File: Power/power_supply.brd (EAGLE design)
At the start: 100 x 80 mm, 10 parts

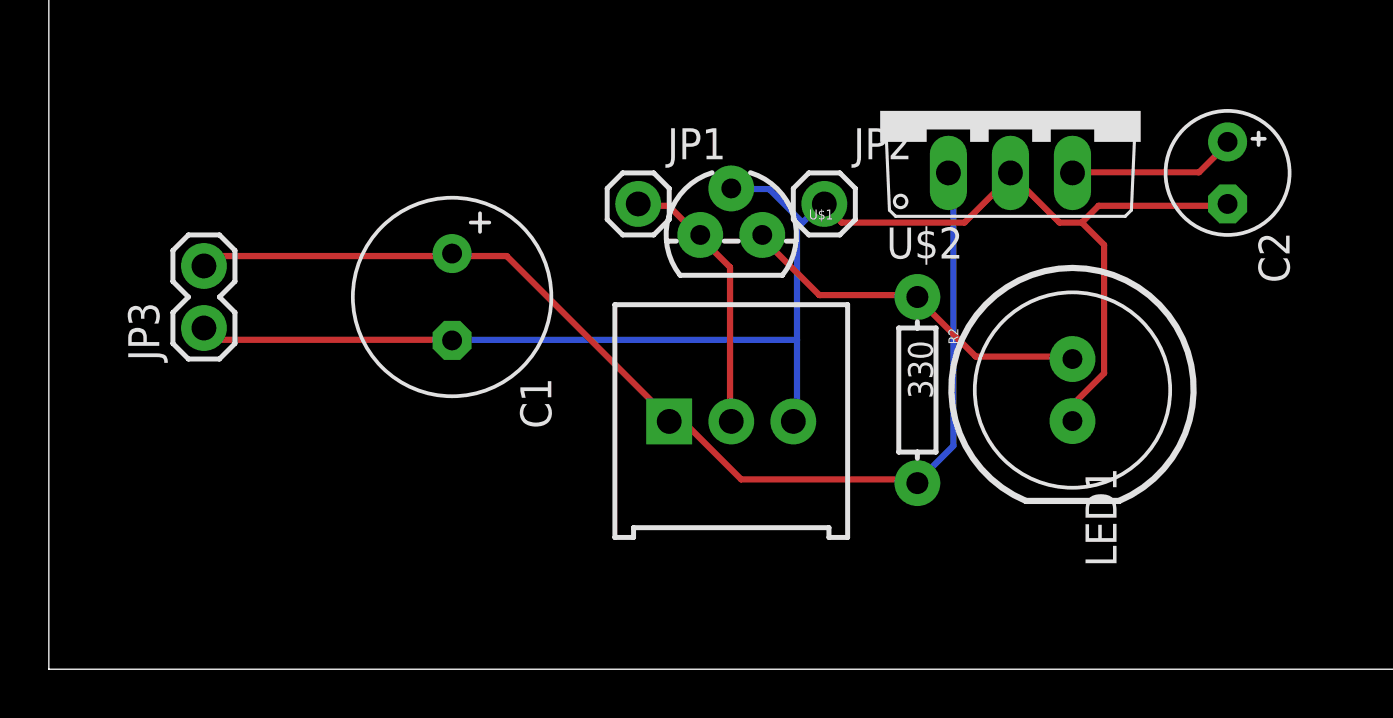
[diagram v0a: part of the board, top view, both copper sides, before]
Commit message: Changes to the Power Supply
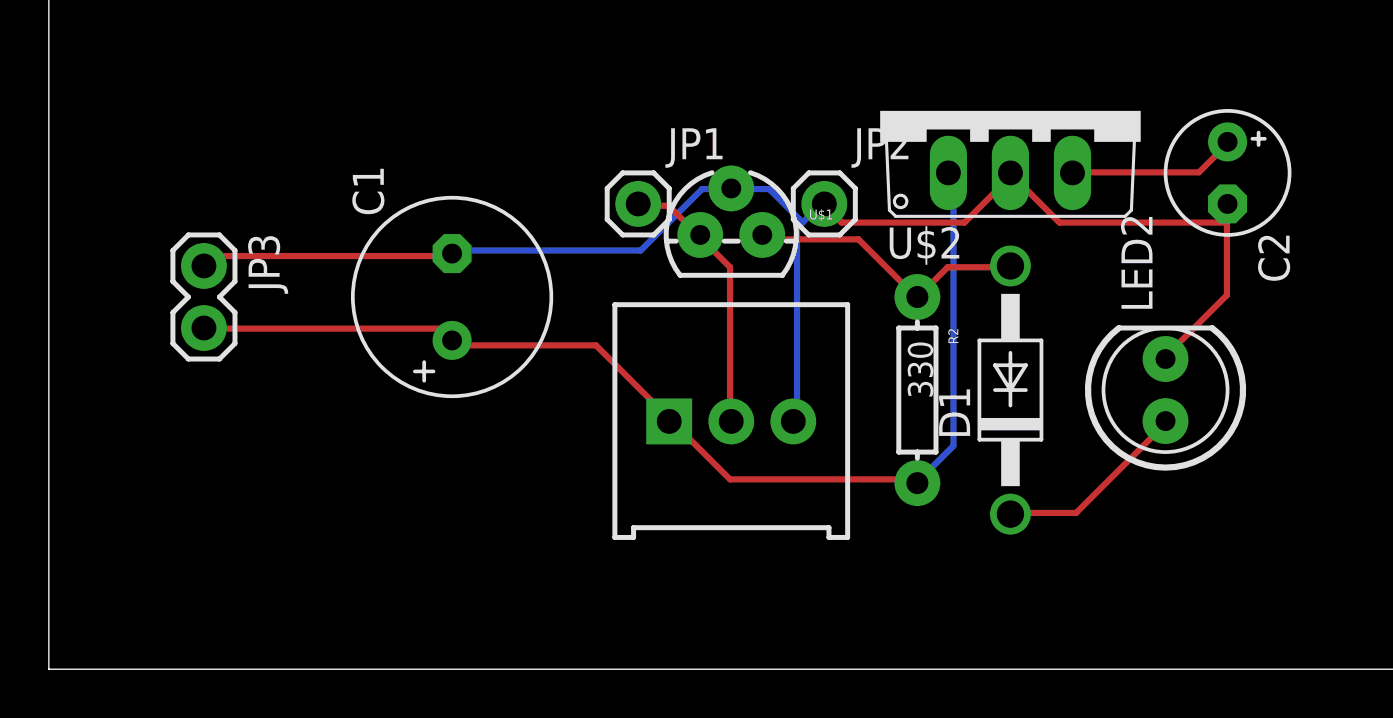
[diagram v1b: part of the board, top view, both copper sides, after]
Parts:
- removed LED1: Green/Yellow, SparkFun:LED10MM-2
- added D1: 1N4001, diode:DO41-10
- added LED2: Yellow/Multi, SparkFun:LED5MM
- moved JP3 2.54 mm to (6.35, 16.5), turned to 270 degrees
- turned C1 to 90 degrees
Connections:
- new net N$1: D1.C, LED2.A
- net GND: now also LED2.K; no longer LED1.K
- net N$2: now also D1.A; no longer LED1.A
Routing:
- net N$1: track 0.00 -> 7.97 mm
- net N$2: track 14.9 -> 11.8 mm
- net GND: track 65.5 -> 62.7 mm
- net VCC: track 46.8 -> 45.3 mm

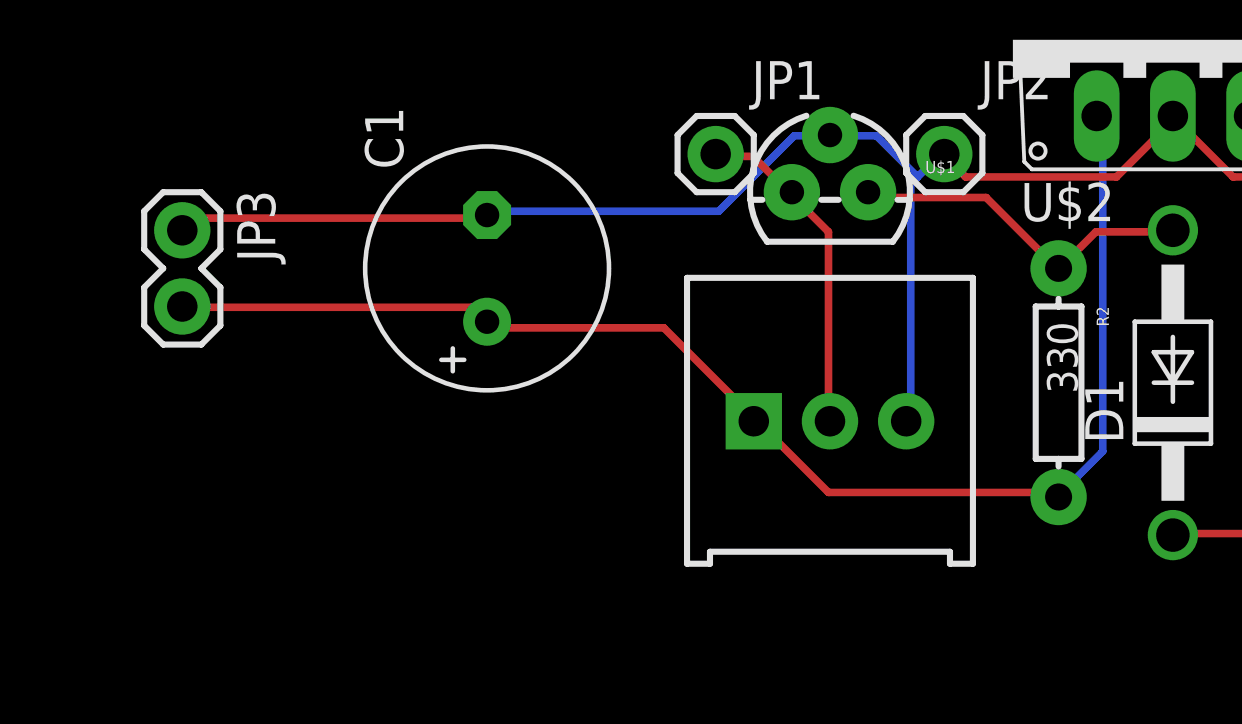
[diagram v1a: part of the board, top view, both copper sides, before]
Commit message: Updated the POT package
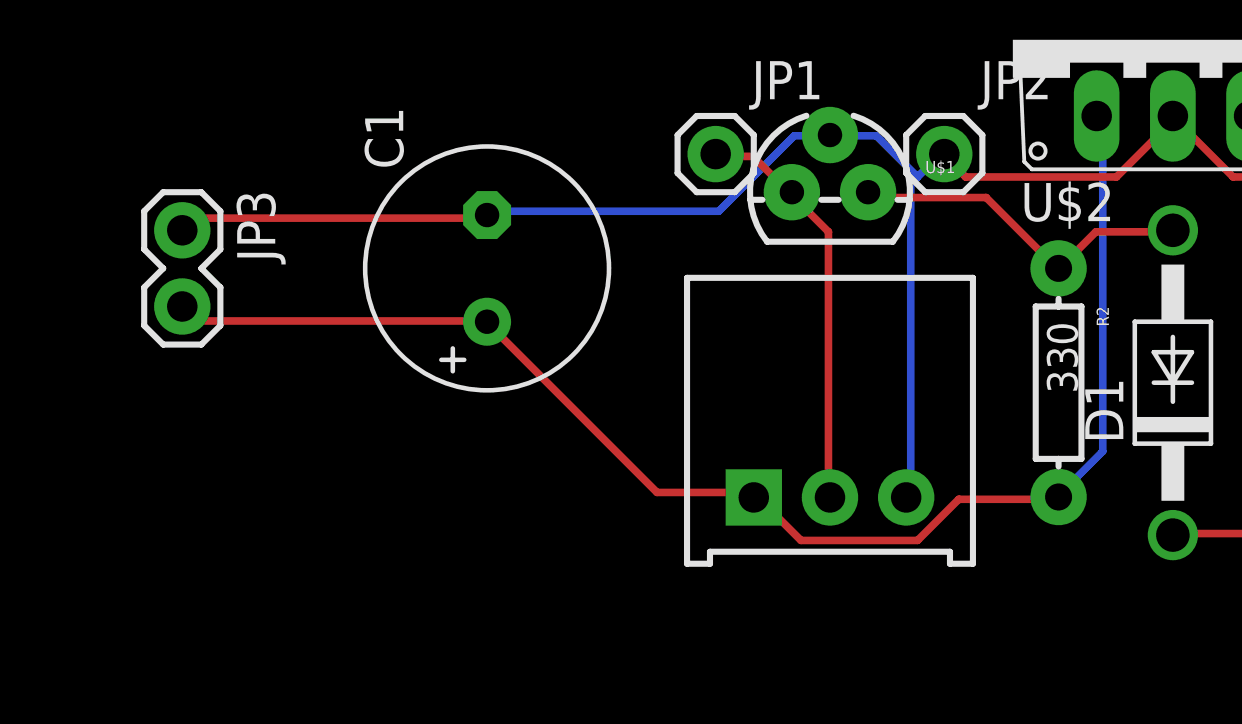
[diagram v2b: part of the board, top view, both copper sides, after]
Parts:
- R1: device SparkFun:3386U -> Power:3386U
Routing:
- net VCUTOFF: track 11.2 -> 13.7 mm
- net GND: track 62.7 -> 65.2 mm
- net VCC: track 45.3 -> 46.5 mm
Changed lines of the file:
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@@
 <element name="JP2" library="SparkFun" package="1X01" value="M01PTH" x="31.75" y="19.05"/>
 <element name="JP3" library="SparkFun" package="1X02" value="Battery" x="6.35" y="16.51" rot="R270"/>
-<element name="R1" library="SparkFun" package="3386U" value="10K" x="27.94" y="10.16"/>
 <element name="R2" library="SparkFun" package="AXIAL-0.3" value="330" x="35.56" y="11.43" rot="R270"/>
 <element name="U$1" library="SparkFun" package="TO-92" value="TL431PTH" x="27.94" y="17.78"/>
@@
 <element name="D1" library="diode" package="DO41-10" value="1N4001" x="39.37" y="11.43" rot="R90"/>
 <element name="LED2" library="SparkFun" package="LED5MM" value="Yellow/Multi" x="45.72" y="11.43" rot="R90"/>
+<element name="R1" library="Power" package="3386U" value="10K" x="27.94" y="10.16">
+<attribute name="CREATOR" value="Brandon" x="27.94" y="10.16" size="1.778" layer="27" display="off"/>
+<attribute name="REVIEWER1" value="Chris" x="27.94" y="10.16" size="1.778" layer="27" display="off"/>
+</element>
 </elements>
 <signals>
@@
 <contactref element="JP2" pad="1"/>
 <contactref element="U$1" pad="2"/>
-<contactref element="R1" pad="3"/>
 <contactref element="JP3" pad="1"/>
 <contactref element="U$2" pad="2"/>
@@
 <contactref element="C2" pad="-"/>
 <contactref element="LED2" pad="K"/>
+<contactref element="R1" pad="3"/>
 <wire x1="6.6294" y1="16.9164" x2="16.4592" y2="16.9164" width="0.254" layer="1"/>
 <wire x1="6.4008" y1="16.6878" x2="6.6294" y2="16.9164" width="0.254" layer="1"/>
@@
 <wire x1="39.3192" y1="20.1168" x2="39.37" y2="20.32" width="0.254" layer="1"/>
 <wire x1="31.7754" y1="18.9738" x2="31.75" y2="19.05" width="0.254" layer="1"/>
-<wire x1="30.6324" y1="18.0594" x2="30.6324" y2="10.287" width="0.254" layer="16"/>
+<wire x1="30.6324" y1="18.0594" x2="30.6324" y2="7.7724" width="0.254" layer="16"/>
 <wire x1="31.5468" y1="18.9738" x2="30.861" y2="18.288" width="0.254" layer="16"/>
 <wire x1="30.861" y1="18.288" x2="30.6324" y2="18.0594" width="0.254" layer="16"/>
-<wire x1="30.6324" y1="10.287" x2="30.48" y2="10.145" width="0.254" layer="16"/>
+<wire x1="30.6324" y1="7.7724" x2="30.48" y2="7.605" width="0.254" layer="16"/>
 <wire x1="31.5468" y1="18.9738" x2="31.75" y2="19.05" width="0.254" layer="16"/>
 <wire x1="29.4894" y1="19.6596" x2="28.1178" y2="19.6596" width="0.254" layer="16"/>
@@
 </signal>
 <signal name="VCUTOFF">
-<contactref element="R1" pad="2"/>
 <contactref element="U$1" pad="1"/>
 <contactref element="JP1" pad="1"/>
+<contactref element="R1" pad="2"/>
 <wire x1="25.3746" y1="18.9738" x2="24.2316" y2="18.9738" width="0.254" layer="1"/>
 <wire x1="26.5176" y1="17.8308" x2="25.3746" y2="18.9738" width="0.254" layer="1"/>
 <wire x1="24.2316" y1="18.9738" x2="24.13" y2="19.05" width="0.254" layer="1"/>
 <wire x1="26.5176" y1="17.8308" x2="26.67" y2="17.78" width="0.254" layer="1"/>
-<wire x1="27.8892" y1="16.4592" x2="27.8892" y2="10.287" width="0.254" layer="1"/>
+<wire x1="27.8892" y1="16.4592" x2="27.8892" y2="7.7724" width="0.254" layer="1"/>
 <wire x1="26.7462" y1="17.6022" x2="27.8892" y2="16.4592" width="0.254" layer="1"/>
-<wire x1="27.8892" y1="10.287" x2="27.94" y2="10.145" width="0.254" layer="1"/>
+<wire x1="27.8892" y1="7.7724" x2="27.94" y2="7.605" width="0.254" layer="1"/>
 <wire x1="26.7462" y1="17.6022" x2="26.67" y2="17.78" width="0.254" layer="1"/>
 </signal>
@@
 <contactref element="JP3" pad="2"/>
 <contactref element="R2" pad="P$2"/>
-<contactref element="R1" pad="1"/>
 <contactref element="U$2" pad="1"/>
 <contactref element="C1" pad="+"/>
+<contactref element="R1" pad="1"/>
 <wire x1="37.0332" y1="9.144" x2="37.0332" y2="20.1168" width="0.254" layer="16"/>
 <wire x1="35.6616" y1="7.7724" x2="37.0332" y2="9.144" width="0.254" layer="16"/>
 <wire x1="37.0332" y1="20.1168" x2="36.83" y2="20.32" width="0.254" layer="16"/>
 <wire x1="35.6616" y1="7.7724" x2="35.56" y2="7.62" width="0.254" layer="16"/>
-<wire x1="22.4028" y1="13.2588" x2="16.6878" y2="13.2588" width="0.254" layer="1"/>
-<wire x1="25.3746" y1="10.287" x2="22.4028" y2="13.2588" width="0.254" layer="1"/>
+<wire x1="6.858" y1="13.4874" x2="16.4592" y2="13.4874" width="0.254" layer="1"/>
+<wire x1="6.4008" y1="13.9446" x2="6.858" y2="13.4874" width="0.254" layer="1"/>
+<wire x1="16.4592" y1="13.4874" x2="16.51" y2="13.462" width="0.254" layer="1"/>
+<wire x1="6.4008" y1="13.9446" x2="6.35" y2="13.97" width="0.254" layer="1"/>
+<wire x1="22.1742" y1="7.7724" x2="25.3746" y2="7.7724" width="0.254" layer="1"/>
+<wire x1="16.6878" y1="13.2588" x2="22.1742" y2="7.7724" width="0.254" layer="1"/>
+<wire x1="25.3746" y1="7.7724" x2="25.4" y2="7.605" width="0.254" layer="1"/>
 <wire x1="16.6878" y1="13.2588" x2="16.51" y2="13.462" width="0.254" layer="1"/>
-<wire x1="25.3746" y1="10.287" x2="25.4" y2="10.145" width="0.254" layer="1"/>
-<wire x1="16.002" y1="13.9446" x2="6.4008" y2="13.9446" width="0.254" layer="1"/>
-<wire x1="16.4592" y1="13.4874" x2="16.002" y2="13.9446" width="0.254" layer="1"/>
-<wire x1="6.4008" y1="13.9446" x2="6.35" y2="13.97" width="0.254" layer="1"/>
-<wire x1="16.4592" y1="13.4874" x2="16.51" y2="13.462" width="0.254" layer="1"/>
-<wire x1="27.8892" y1="7.7724" x2="35.433" y2="7.7724" width="0.254" layer="1"/>
-<wire x1="25.6032" y1="10.0584" x2="27.8892" y2="7.7724" width="0.254" layer="1"/>
-<wire x1="35.433" y1="7.7724" x2="35.56" y2="7.62" width="0.254" layer="1"/>
-<wire x1="25.6032" y1="10.0584" x2="25.4" y2="10.145" width="0.254" layer="1"/>
+<wire x1="32.2326" y1="7.5438" x2="35.433" y2="7.5438" width="0.254" layer="1"/>
+<wire x1="30.861" y1="6.1722" x2="32.2326" y2="7.5438" width="0.254" layer="1"/>
+<wire x1="26.9748" y1="6.1722" x2="30.861" y2="6.1722" width="0.254" layer="1"/>
+<wire x1="25.6032" y1="7.5438" x2="26.9748" y2="6.1722" width="0.254" layer="1"/>
+<wire x1="35.433" y1="7.5438" x2="35.56" y2="7.62" width="0.254" layer="1"/>
+<wire x1="25.6032" y1="7.5438" x2="25.4" y2="7.605" width="0.254" layer="1"/>
 </signal>
 <signal name="VDD">
